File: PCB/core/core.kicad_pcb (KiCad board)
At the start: 2 copper layers, 100 x 100 mm, 43 parts, among them U1 MCU_Seeed_XIAO_ESP32-C3, U2 STP55NF06L

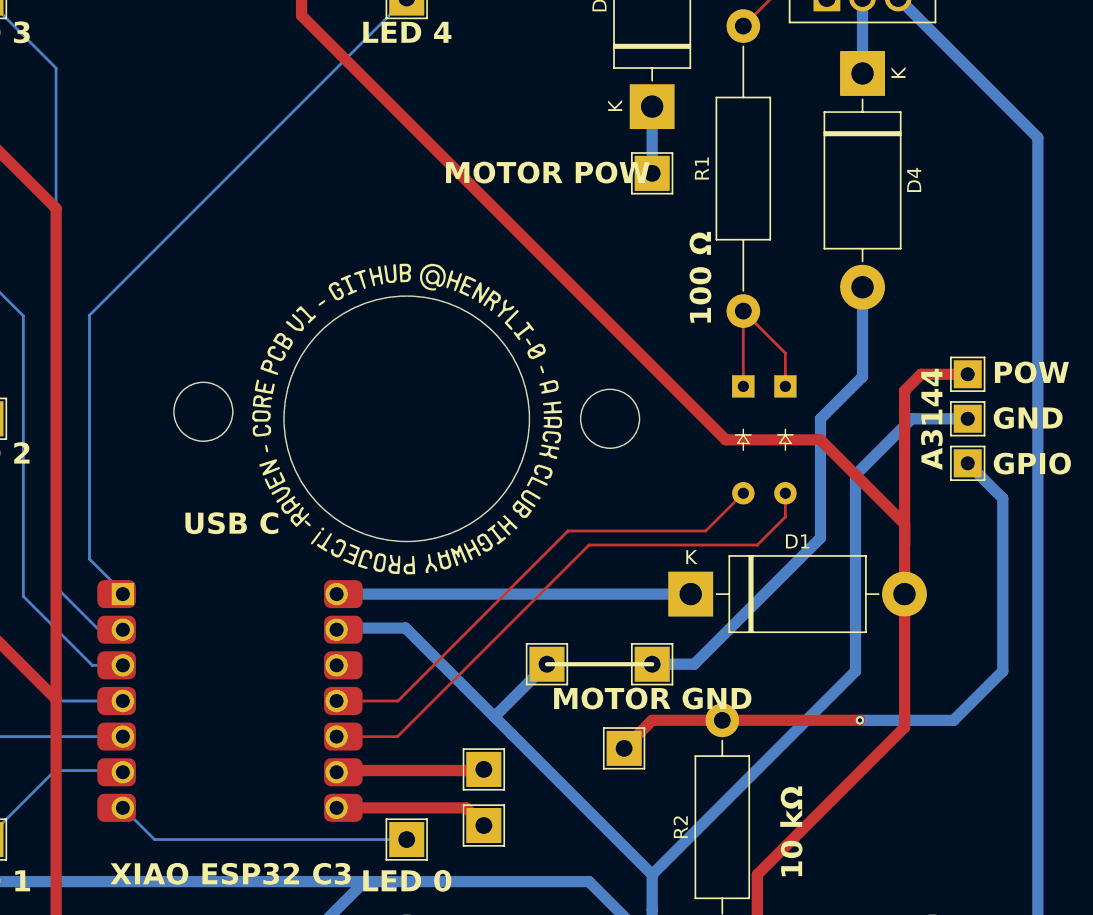
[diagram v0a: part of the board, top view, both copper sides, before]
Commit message: update led panel and step files
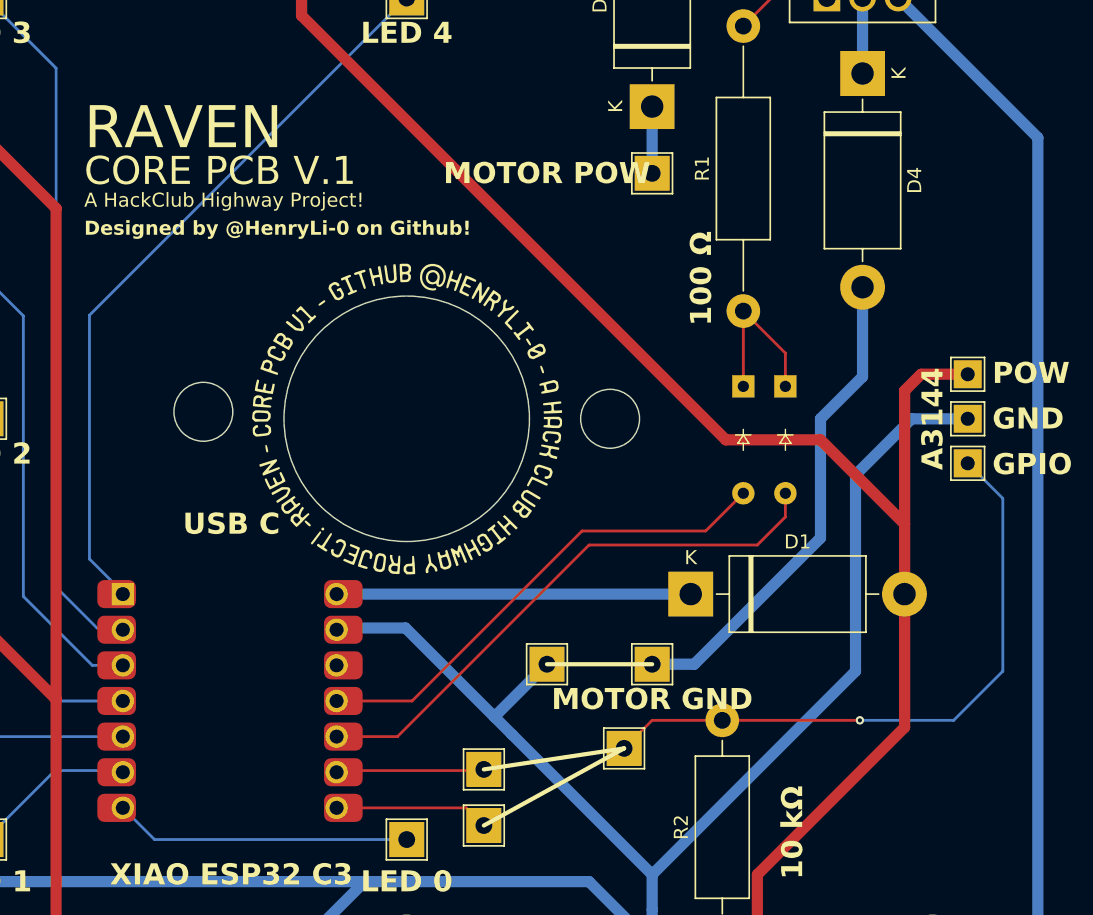
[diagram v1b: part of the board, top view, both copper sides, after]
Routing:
- net A3114E POW: track 303.4 -> 301.9 mm
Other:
- board text added: "A HackClub Highway Project!"
- board text added: "CORE PCB V.1"
- board text added: "Designed by @HenryLi-0 on Github!"
- board text added: "RAVEN"

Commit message: im tired
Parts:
- removed the REF** at (167.5, 117.5)
- removed the REF** at (150.0, 70.0)
- removed the REF** at (120.0, 57.5)
- removed the REF** at (142.5, 62.5)
- removed the REF** at (107.5, 67.5)
- removed the REF** at (155.5, 125.0)
- removed the REF** at (112.5, 117.5)
- removed the REF** at (160.0, 117.5)
- removed the REF** at (120.0, 130.0)
- removed the REF** at (165.5, 123.5)
- removed the REF** at (167.5, 145.0)
- removed the REF** at (175.0, 145.0)
- removed the REF** at (120.0, 100.0)
- removed the REF** at (175.0, 55.0)
- removed the REF** at (112.5, 107.5)
- removed the REF** at (190.0, 103.2)
- removed the REF** at (190.0, 96.8)
- removed the REF** at (107.5, 132.5)
- removed the REF** at (142.5, 137.5)
- removed the REF** at (182.5, 145.0)
- removed the REF** at (167.5, 82.5)
- removed the REF** at (167.5, 55.0)
- removed the REF** at (112.5, 92.5)
- removed the REF** at (117.5, 142.5)
- removed the REF** at (120.0, 70.0)
- removed the REF** at (182.5, 55.0)
- removed the REF** at (190.0, 100.0)
- removed the REF** at (155.5, 129.0)
- removed the REF** at (157.5, 137.5)
- removed the REF** at (157.5, 62.5)
- removed the REF** at (112.5, 82.5)
- removed the REF** at (150.0, 130.0)
- added ?: , , F.Cu at (157.5, 62.0)
- added ?: , , F.Cu at (120.0, 69.5)
- added ?: , , F.Cu at (142.5, 62.0)
- added ?: , , F.Cu at (150.0, 69.5)
- added REF**: TestPoint_THTPad_2.5x2.5mm_Drill1.2mm, TestPoint:TestPoint_THTPad_2.5x2.5mm_Drill1.2mm, F.Cu at (120.0, 57.0)
- added REF**: TestPoint_THTPad_2.5x2.5mm_Drill1.2mm, TestPoint:TestPoint_THTPad_2.5x2.5mm_Drill1.2mm, F.Cu at (150.0, 69.5)
- added REF**: TestPoint_THTPad_2.5x2.5mm_Drill1.2mm, TestPoint:TestPoint_THTPad_2.5x2.5mm_Drill1.2mm, F.Cu at (142.5, 62.0)
- added REF**: TestPoint_THTPad_2.5x2.5mm_Drill1.2mm, TestPoint:TestPoint_THTPad_2.5x2.5mm_Drill1.2mm, F.Cu at (157.5, 62.0)
- added REF**: TestPoint_THTPad_2.5x2.5mm_Drill1.2mm, TestPoint:TestPoint_THTPad_2.5x2.5mm_Drill1.2mm, F.Cu at (120.0, 69.5)
- added REF**: TestPoint_THTPad_2.5x2.5mm_Drill1.2mm, TestPoint:TestPoint_THTPad_2.5x2.5mm_Drill1.2mm, F.Cu at (107.5, 67.0)
- moved U2 86.9 mm to (243.7, 129.0)
- moved D3 64.0 mm to (221.5, 112.1), turned to 0 degrees
- moved D2 61.2 mm to (223.8, 137.0)
- moved D5 59.3 mm to (220.8, 134.1)
- moved D4 58.4 mm to (221.5, 118.9), turned to 0 degrees
- moved R1 47.6 mm to (221.1, 99.4), turned to 0 degrees
- moved R2 24.0 mm to (194.0, 126.1)
- moved D1 14.9 mm to (155.4, 112.5)
- moved U1 3.05 mm to (135.0, 122.0)
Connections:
- U2 pad 3: M_GND -> A3144E GND
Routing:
- net A3114E POW: track 301.9 -> 0.00 mm
- net A3144E GND: track 295.2 -> 0.00 mm
- net M_GND: track 106.4 -> 0.00 mm
- net A3144E GPIO: track 66.7 -> 0.12 mm, vias 1 -> 0
- net LED_4: track 52.9 -> 0.00 mm
- net LED_3: track 49.6 -> 0.00 mm
- net LED_BACKUP_2: track 43.1 -> 0.00 mm
- net Net-(D2-A): track 40.6 -> 0.00 mm
- net MOTOR-: track 35.6 -> 0.00 mm
- net Net-(D5-A): track 35.1 -> 0.00 mm
- net LED_2: track 26.5 -> 0.00 mm
- net Net-(D1-K): track 25.8 -> 0.00 mm
- net LED_0: track 21.4 -> 0.00 mm
- net LED_BACKUP_1: track 19.5 -> 0.00 mm
- net Net-(D2-K): track 12.0 -> 0.00 mm
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- removed copper zone on B.Cu, net A3144E GND
- removed copper zone on F.Cu, net A3144E GND
